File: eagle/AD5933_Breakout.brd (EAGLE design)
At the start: 25.4 x 20.3 mm, 5 parts, among them U1 AD5933

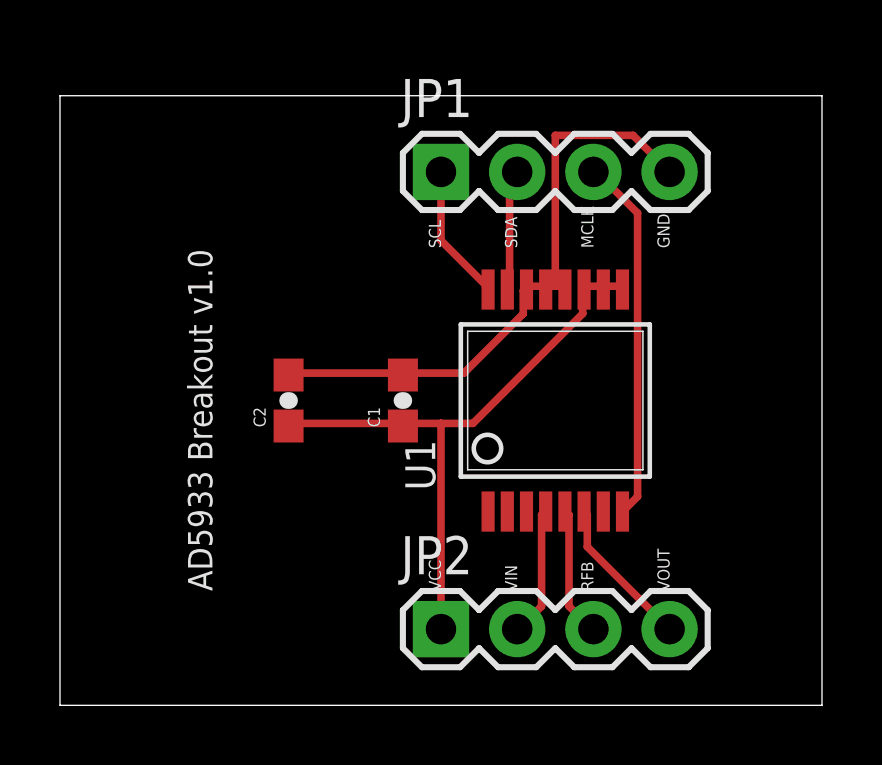
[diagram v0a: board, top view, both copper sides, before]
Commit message: added top and bottom copper pours to pcb
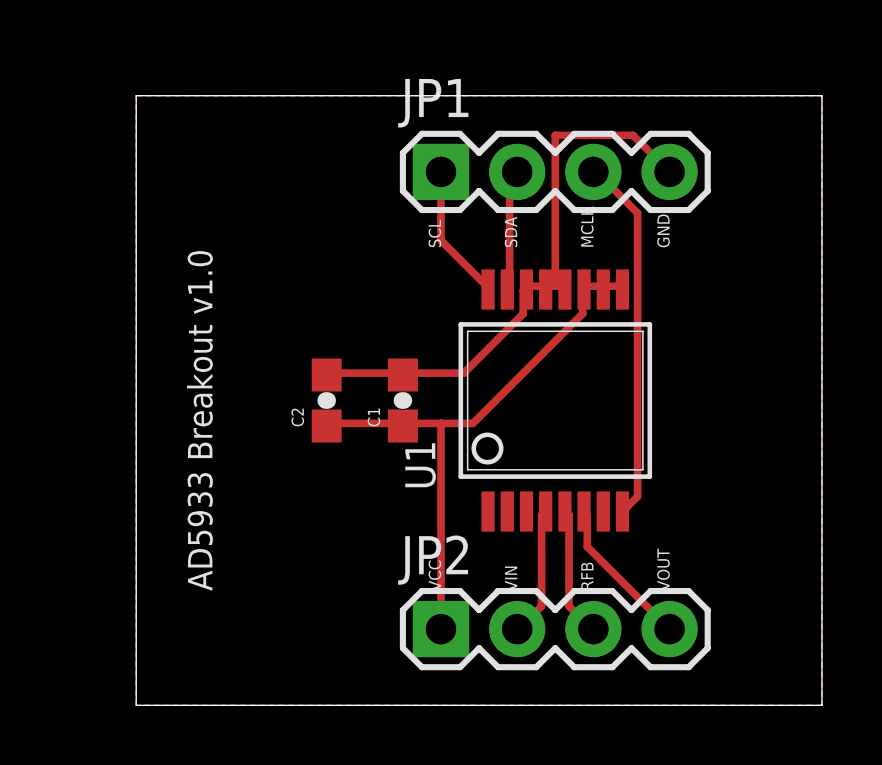
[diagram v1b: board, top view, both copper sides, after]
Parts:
- moved C2 1.27 mm to (11.4, 11.4)
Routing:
- net GND: track 20.5 -> 19.3 mm
- net VCC: track 20.6 -> 19.4 mm
- added copper zone on layer 1, net GND
- added copper zone on layer 16, net GND
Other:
- board size 25.4 x 20.3 mm -> 22.9 x 20.3 mm
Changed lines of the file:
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@@
 <?xml version="1.0" encoding="utf-8"?>
 <!DOCTYPE eagle SYSTEM "eagle.dtd">
-<eagle version="6.4">
+<eagle version="6.5.0">
 <drawing>
 <settings>
@@
 <board>
 <plain>
-<wire x1="2.54" y1="1.27" x2="27.94" y2="1.27" width="0" layer="20"/>
+<wire x1="5.08" y1="1.27" x2="27.94" y2="1.27" width="0" layer="20"/>
 <wire x1="27.94" y1="1.27" x2="27.94" y2="21.59" width="0" layer="20"/>
-<wire x1="27.94" y1="21.59" x2="2.54" y2="21.59" width="0" layer="20"/>
-<wire x1="2.54" y1="21.59" x2="2.54" y2="1.27" width="0" layer="20"/>
+<wire x1="27.94" y1="21.59" x2="5.08" y2="21.59" width="0" layer="20"/>
+<wire x1="5.08" y1="21.59" x2="5.08" y2="1.27" width="0" layer="20"/>
 <text x="15.24" y="16.51" size="0.4064" layer="21" font="vector" ratio="15" rot="R90">SCL</text>
 <text x="17.78" y="16.51" size="0.4064" layer="21" font="vector" ratio="15" rot="R90">SDA</text>
@@
 <attribute name="PROD_ID" value="CAP-08390" x="35.56" y="49.53" size="1.778" layer="27" rot="R90" display="off"/>
 </element>
-<element name="C2" library="SparkFun-Capacitors" package="0603-CAP" value="10uF" x="10.16" y="11.43" rot="R90">
-<attribute name="PROD_ID" value="CAP-08390" x="31.75" y="53.34" size="1.778" layer="27" rot="R90" display="off"/>
+<element name="C2" library="SparkFun-Capacitors" package="0603-CAP" value="10uF" x="11.43" y="11.43" rot="R90">
+<attribute name="PROD_ID" value="CAP-08390" x="33.02" y="53.34" size="1.778" layer="27" rot="R90" display="off"/>
 </element>
 <element name="JP1" library="SparkFun-Connectors" package="1X04" value="" x="15.24" y="19.05"/>
@@
 <wire x1="19.3548" y1="15.24" x2="19.37" y2="15.13" width="0.254" layer="1"/>
 <wire x1="18.7452" y1="15.24" x2="18.73" y2="15.13" width="0.254" layer="1"/>
-<wire x1="13.8684" y1="12.3444" x2="10.2108" y2="12.3444" width="0.254" layer="1"/>
-<wire x1="10.2108" y1="12.3444" x2="10.16" y2="12.28" width="0.254" layer="1"/>
+<wire x1="13.8684" y1="12.3444" x2="11.43" y2="12.3444" width="0.254" layer="1"/>
+<wire x1="11.43" y1="12.3444" x2="11.43" y2="12.28" width="0.254" layer="1"/>
 <wire x1="13.8684" y1="12.3444" x2="13.97" y2="12.28" width="0.254" layer="1"/>
 <wire x1="17.9832" y1="14.3256" x2="17.9832" y2="15.0876" width="0.254" layer="1"/>
@@
 <wire x1="19.05" y1="20.2692" x2="21.6408" y2="20.2692" width="0.254" layer="1"/>
 <wire x1="19.05" y1="15.24" x2="19.05" y2="20.2692" width="0.254" layer="1"/>
+<polygon width="0.254" layer="1" isolate="0.3048" orphans="yes">
+<vertex x="5.08" y="21.59"/>
+<vertex x="27.94" y="21.59"/>
+<vertex x="27.94" y="1.27"/>
+<vertex x="5.08" y="1.27"/>
+</polygon>
+<polygon width="0.254" layer="16" isolate="0.3048" orphans="yes">
+<vertex x="5.08" y="21.59"/>
+<vertex x="27.94" y="21.59"/>
+<vertex x="27.94" y="1.27"/>
+<vertex x="5.08" y="1.27"/>
+</polygon>
 </signal>
 <signal name="SCL">
@@
 <wire x1="21.1836" y1="15.24" x2="21.29" y2="15.13" width="0.254" layer="1"/>
 <wire x1="20.7264" y1="15.24" x2="20.65" y2="15.13" width="0.254" layer="1"/>
-<wire x1="13.8684" y1="10.668" x2="10.2108" y2="10.668" width="0.254" layer="1"/>
-<wire x1="10.2108" y1="10.668" x2="10.16" y2="10.58" width="0.254" layer="1"/>
+<wire x1="13.8684" y1="10.668" x2="11.43" y2="10.668" width="0.254" layer="1"/>
+<wire x1="11.43" y1="10.668" x2="11.43" y2="10.58" width="0.254" layer="1"/>
 <wire x1="13.8684" y1="10.668" x2="13.97" y2="10.58" width="0.254" layer="1"/>
 <wire x1="19.9644" y1="14.3256" x2="19.9644" y2="15.0876" width="0.254" layer="1"/>

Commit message: created new gerber files
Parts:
- moved C2 12.0 mm to (21.6, 17.8)
- moved C1 8.98 mm to (20.3, 17.8)
- moved JP1 6.35 mm to (8.89, 19.1)
- moved JP2 6.35 mm to (8.89, 3.81)
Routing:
- net MCLK: track 12.2 -> 22.1 mm
- net GND: track 19.3 -> 11.0 mm
- net SCL: track 4.56 -> 11.8 mm
- net RFB: track 4.35 -> 10.3 mm
- net SDA: track 4.11 -> 8.82 mm
- net VIN: track 4.35 -> 8.15 mm
- net VCC: track 19.4 -> 22.5 mm
